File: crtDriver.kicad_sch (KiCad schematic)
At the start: 11 parts

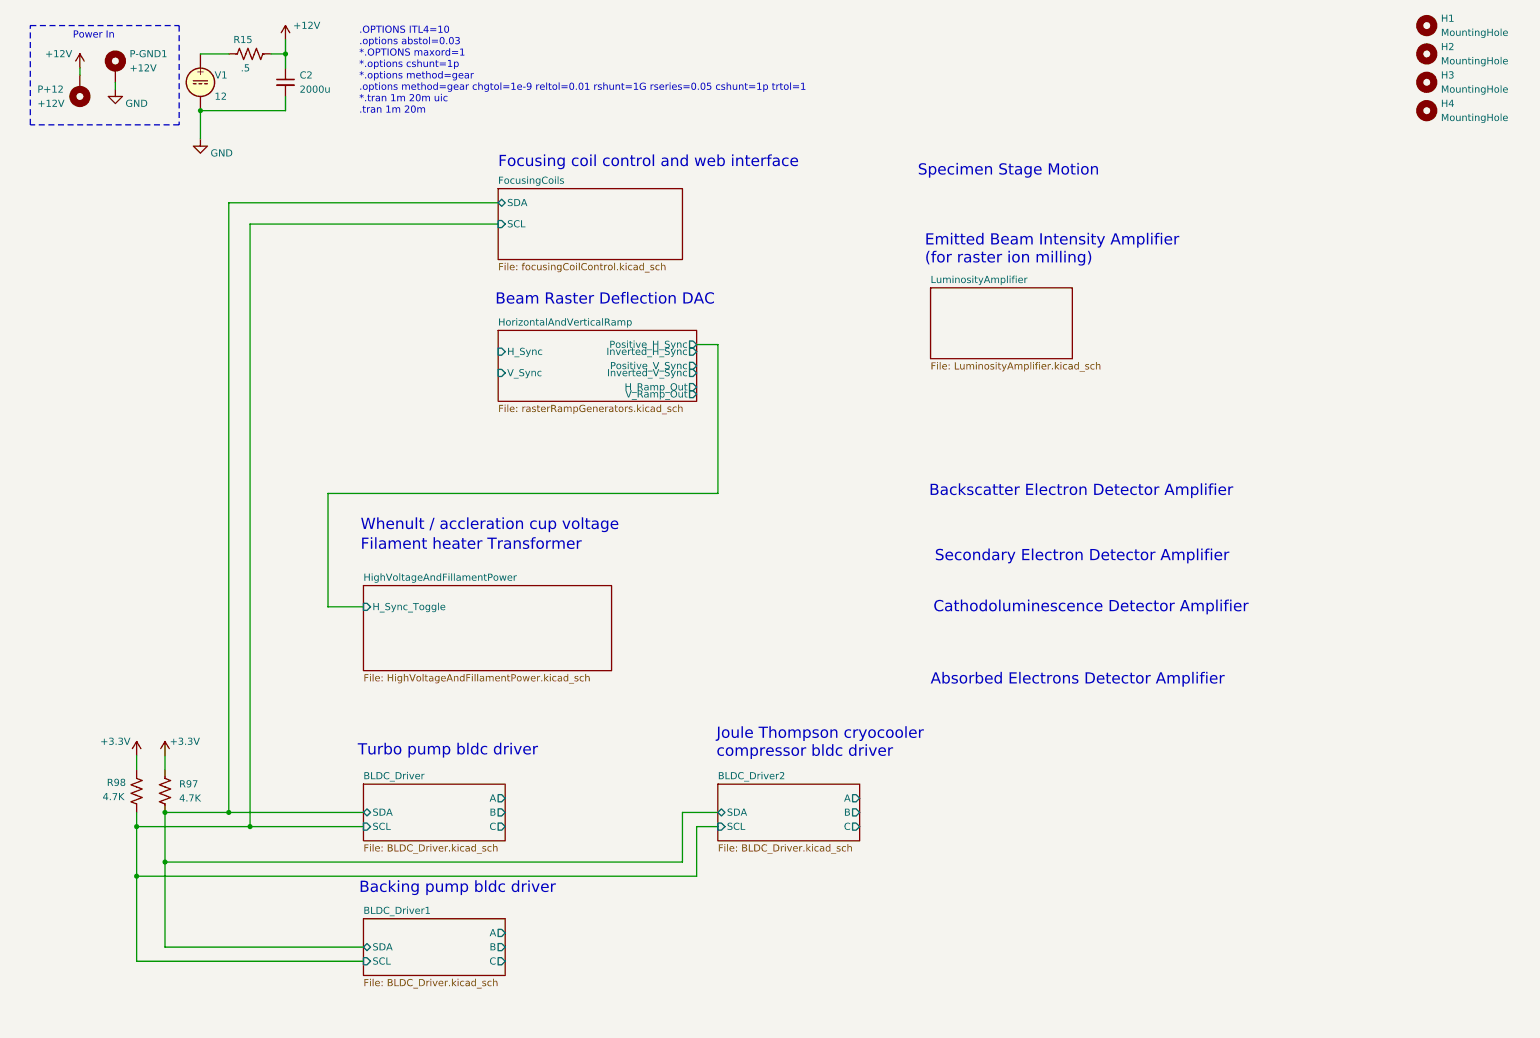
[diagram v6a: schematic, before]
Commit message: added more labels of components to top level schematic
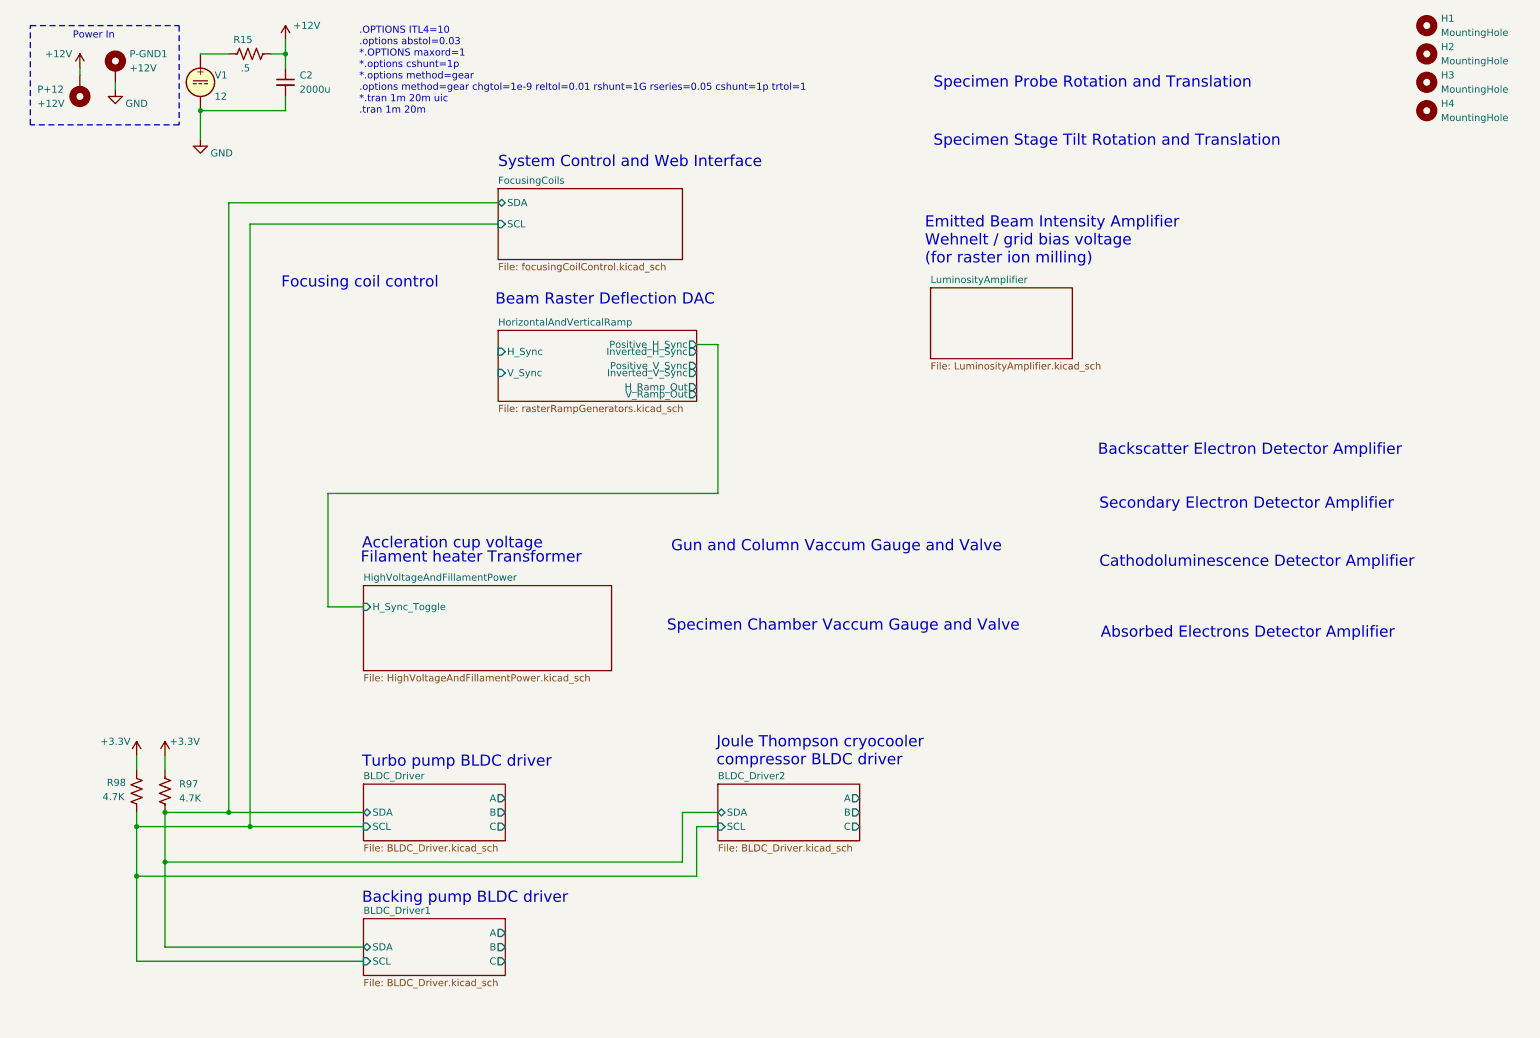
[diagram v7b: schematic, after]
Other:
- note added: "Accleration cup voltage"
- note added: "Backing pump BLDC driver"
- note added: "Emitted Beam Intensity Amplifier Wehnelt / grid bias voltage (for raster ion milling)"
- note added: "Focusing coil control"
- note added: "Gun and Column Vaccum Gauge and Valve"
- note added: "Joule Thompson cryocooler compressor BLDC driver"
- note added: "Specimen Chamber Vaccum Gauge and Valve"
- note added: "Specimen Probe Rotation and Translation"
- note added: "Specimen Stage Tilt Rotation and Translation"
- note added: "System Control and Web Interface"
- note added: "Turbo pump BLDC driver"
- note removed: "Backing pump bldc driver"
- note removed: "Emitted Beam Intensity Amplifier (for raster ion milling)"
- note removed: "Focusing coil control and web interface"
- note removed: "Joule Thompson cryocooler compressor bldc driver"
- note removed: "Specimen Stage Motion"
- note removed: "Turbo pump bldc driver"
- note removed: "Whenult / accleration cup voltage"
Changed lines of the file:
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@@
 		)
 	)
-	(text "Secondary Electron Detector Amplifier"
+	(text "Specimen Chamber Vaccum Gauge and Valve"
 		(exclude_from_sim no)
-		(at 178.562 112.776 0)
+		(at 130.556 125.222 0)
 		(effects
 			(font
@@
 		)
 	)
-	(text "Joule Thompson cryocooler\ncompressor bldc driver"
+	(text "Secondary Electron Detector Amplifier"
 		(exclude_from_sim no)
-		(at 139.446 147.828 0)
+		(at 208.026 103.378 0)
 		(effects
 			(font
@@
 		)
 	)
-	(text "Turbo pump bldc driver"
+	(text "Joule Thompson cryocooler\ncompressor BLDC driver"
 		(exclude_from_sim no)
-		(at 75.184 147.574 0)
+		(at 139.446 149.352 0)
 		(effects
 			(font
@@
 		)
 	)
-	(text "Specimen Stage Motion"
+	(text "Turbo pump BLDC driver"
 		(exclude_from_sim no)
-		(at 175.514 43.688 0)
+		(at 75.946 149.606 0)
 		(effects
 			(font
@@
 		)
 	)
-	(text "Whenult / accleration cup voltage"
+	(text "Specimen Stage Tilt Rotation and Translation"
 		(exclude_from_sim no)
-		(at 75.692 107.188 0)
+		(at 178.308 38.354 0)
 		(effects
 			(font
@@
 		)
 	)
-	(text "Backing pump bldc driver"
+	(text "Accleration cup voltage"
 		(exclude_from_sim no)
-		(at 75.438 172.212 0)
+		(at 75.946 110.49 0)
+		(effects
+			(font
+				(size 2 2)
+			)
+			(justify left bottom)
+		)
+	)
+	(text "Backing pump BLDC driver"
+		(exclude_from_sim no)
+		(at 75.946 173.99 0)
 		(effects
 			(font
@@
 		)
 	)
+	(text "Gun and Column Vaccum Gauge and Valve"
+		(exclude_from_sim no)
+		(at 131.318 110.998 0)
+		(effects
+			(font
+				(size 2 2)
+			)
+			(justify left bottom)
+		)
+	)
+	(text "Focusing coil control"
+		(exclude_from_sim no)
+		(at 61.468 63.754 0)
+		(effects
+			(font
+				(size 2 2)
+			)
+			(justify left bottom)
+		)
+	)
+	(text "Specimen Probe Rotation and Translation"
+		(exclude_from_sim no)
+		(at 178.308 27.94 0)
+		(effects
+			(font
+				(size 2 2)
+			)
+			(justify left bottom)
+		)
+	)
 	(text "Filament heater Transformer"
 		(exclude_from_sim no)
-		(at 75.692 110.744 0)
+		(at 75.692 113.03 0)
 		(effects
 			(font
@@
 	(text "Cathodoluminescence Detector Amplifier"
 		(exclude_from_sim no)
-		(at 178.308 121.92 0)
+		(at 208.026 113.792 0)
 		(effects
 			(font
@@
 	(text "Backscatter Electron Detector Amplifier"
 		(exclude_from_sim no)
-		(at 177.546 101.092 0)
+		(at 207.772 93.726 0)
 		(effects
 			(font
@@
 		)
 	)
-	(text "Emitted Beam Intensity Amplifier\n(for raster ion milling)"
+	(text "Emitted Beam Intensity Amplifier\nWehnelt / grid bias voltage\n(for raster ion milling)"
 		(exclude_from_sim no)
 		(at 176.784 59.436 0)
@@
 		)
 	)
-	(text "Focusing coil control and web interface"
+	(text "System Control and Web Interface"
 		(exclude_from_sim no)
 		(at 100.33 42.164 0)
@@
 	(text "Absorbed Electrons Detector Amplifier"
 		(exclude_from_sim no)
-		(at 177.8 134.874 0)
+		(at 208.28 126.492 0)
 		(effects
 			(font
